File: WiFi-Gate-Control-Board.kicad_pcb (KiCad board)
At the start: 4 copper layers, 139.7 x 158.8 mm, 259 parts, among them J1 USB_B_Micro, J10 Screw_Terminal_01x02, J11 Screw_Terminal_01x04, J12 Screw_Terminal_01x04, J2 Cortex Debug, J3 Motor, J4 Screw_Terminal_01x04, J5 Screw_Terminal_01x04, J6 Screw_Terminal_01x04, J7 Screw_Terminal_01x04, J8 Screw_Terminal_01x04, J9 Screw_Terminal_01x04, Q1 IPD90P03P4L-04, Q2 IFX007T, Q3 IFX007T, SW1 LED Enable, SW2 Open-Close, U1 LMZ21700, U10 TPS3779, U11 TPS3779, U12 TPS3779, U13 TPS3779, U14 TCA6424A, U15 REF3330, U16 TPS3779, U17 TPS3779, U18 TPS3779, U19 TPS3779, U2 DS18B20U, U20 TPS3779, U21 TPS3779, U22 TPS3779, U23 TPS3779, U24 LMZ21700, U25 LP5024, U26 TCA6408A, U27 ITS4075Q, U3 ATWINC1500-MR210UB, U4 SAMD21G18-M, U5 74LVC2G07, U6 74LVC2G06, U7 74LVC2G17, U8 74LVC1G04, U9 REF3325, Y1 32.768kHz

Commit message: Rev 1.0 Release
Added input design and calculations. Added BOM. Added Fuse 3D Model.
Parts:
- removed the J11 at (218.8, 173.2)
- removed the J6 at (106.4, 164.3)
- added J5: Screw_Terminal_01x04, Connector_Phoenix_MSTB:PhoenixContact_MSTBVA_2,5_4-G-5,08_1x04_P5.08mm_Vertical, F.Cu at (106.4, 164.3)
- added J9: Screw_Terminal_01x02, Connector_Phoenix_MSTB:PhoenixContact_MSTBVA_2,5_2-G-5,08_1x02_P5.08mm_Vertical, F.Cu at (194.6, 199.2)
- D28: renamed from D7; footprint Package_TO_SOT_SMD:SOT-23 -> Package_TO_SOT_SMD:SOT-323_SC-70
- J10: value Screw_Terminal_01x02 -> Screw_Terminal_01x04; footprint Connector_Phoenix_MSTB:PhoenixContact_MSTBVA_2,5_2-G-5,08_1x02_P5.08mm_Vertical -> Connector_Phoenix_MSTB:PhoenixContact_MSTBVA_2,5_4-G-5,08_1x04_P5.08mm_Vertical
- Z1: footprint Diode_SMD:D_SOD-523 -> Diode_SMD:D_SOT-23_ANK
- moved J10 35.5 mm to (218.8, 173.2), turned to 270 degrees
- moved Z1 2.43 mm to (175.2, 65.9), turned to 0 degrees
- renumbered C42 to C25, C43 to C26, C44 to C27, C45 to C28, C46 to C29, C47 to C30, C48 to C31, C49 to C32, C50 to C33, C51 to C34, C52 to C35, C53 to C36, C54 to C37, C55 to C38, C56 to C39, C57 to C40, C58 to C41, C59 to C42, C60 to C43, C61 to C44, C62 to C45, C63 to C46, C64 to C47, C65 to C48, C66 to C49, C67 to C50, C68 to C51, C69 to C52, C70 to C53, C71 to C54, C72 to C55, C73 to C56, C74 to C57, C75 to C58, C76 to C59, C77 to C60, C78 to C61, C79 to C62, C80 to C63, C25 to C64, C26 to C65, C27 to C66, C28 to C67, C29 to C68, C30 to C69, C31 to C70, C32 to C71, C33 to C72, C34 to C73, C35 to C74, C36 to C75, C37 to C76, C38 to C77, C39 to C78, C40 to C79, C41 to C80, D11 to D10, D12 to D11, D13 to D12, D14 to D13, D15 to D14, D16 to D15, D17 to D16, D18 to D17, D19 to D18, D20 to D19, D21 to D20, D22 to D21, D23 to D22, D24 to D23, D25 to D24, D26 to D25, D27 to D26, D28 to D27, D8 to D7, D9 to D8, D10 to D9, F2 to F1, F3 to F2, F1 to F3, J12 to J11, J3 to J12, J4 to J3, J5 to J4, J7 to J6, J8 to J7, J9 to J8, R22 to R10, R23 to R11, R24 to R12, R25 to R13, R26 to R14, R27 to R15, R28 to R16, R29 to R17, R30 to R18, R31 to R19, R32 to R20, R33 to R21, R34 to R22, R35 to R23, R36 to R24, R37 to R25, R38 to R26, R39 to R27, R40 to R28, R41 to R29, R42 to R30, R43 to R31, R44 to R32, R45 to R33, R46 to R34, R47 to R35, R48 to R36, R49 to R37, R50 to R38, R51 to R39, R52 to R40, R53 to R41, R54 to R42, R55 to R43, R56 to R44, R57 to R45, R58 to R46, R59 to R47, R60 to R48, R61 to R49, R62 to R50, R63 to R51, R64 to R52, R65 to R53, R66 to R54, R67 to R55, R68 to R56, R69 to R57, R70 to R58, R71 to R59, R72 to R60, R73 to R61, R74 to R62, R75 to R63, R76 to R64, R77 to R65, R78 to R66, R79 to R67, R80 to R68, R81 to R69, R82 to R70, R83 to R71, R84 to R72, R85 to R73, R86 to R74, R10 to R75, R11 to R76, R12 to R77, R13 to R78, R14 to R79, R15 to R80, R16 to R81, R17 to R82, R18 to R83, R19 to R84, R20 to R85, R21 to R86, U13 to U10, U14 to U11, U15 to U12, U16 to U13, U17 to U14, U18 to U15, U19 to U16, U20 to U17, U21 to U18, U22 to U19, U23 to U20, U24 to U21, U25 to U22, U26 to U23, U27 to U24, U7 to U25, U8 to U26, U9 to U27, U10 to U7, U11 to U8, U12 to U9
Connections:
- J10 pad 1: GND -> /Outputs and LEDs/VSW3
- J10 pad 2: /Outputs and LEDs/VSW2 -> GND
- RL1 pad 3: Net-(J11-Pad3) (its old number) -> Net-(J10-Pad3)
- RL1 pad 4: Net-(J11-Pad4) (its old number) -> Net-(J10-Pad4)
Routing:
- net Net-(J11-Pad4) (its old number): track 13.3 -> 0.00 mm
- net Net-(J11-Pad3) (its old number): track 13.3 -> 0.00 mm
- net Net-(J10-Pad4): track 0.00 -> 13.3 mm
- net Net-(J10-Pad3): track 0.00 -> 13.3 mm
- net Net-(D28-Pad1): track 19.8 -> 22.4 mm
- net Net-(Q1-Pad1): track 4.79 -> 6.76 mm
- net GND: track 245.0 -> 246.8 mm, vias 171 -> 252
- net +3.3V: track 135.7 -> 136.3 mm
- net /Inputs/IN11: track 15.8 -> 16.3 mm
- net /Motor Driver/M1B: vias 55 -> 47
- net /Motor Driver/M1A: vias 54 -> 46
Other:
- board text removed: "Radio"

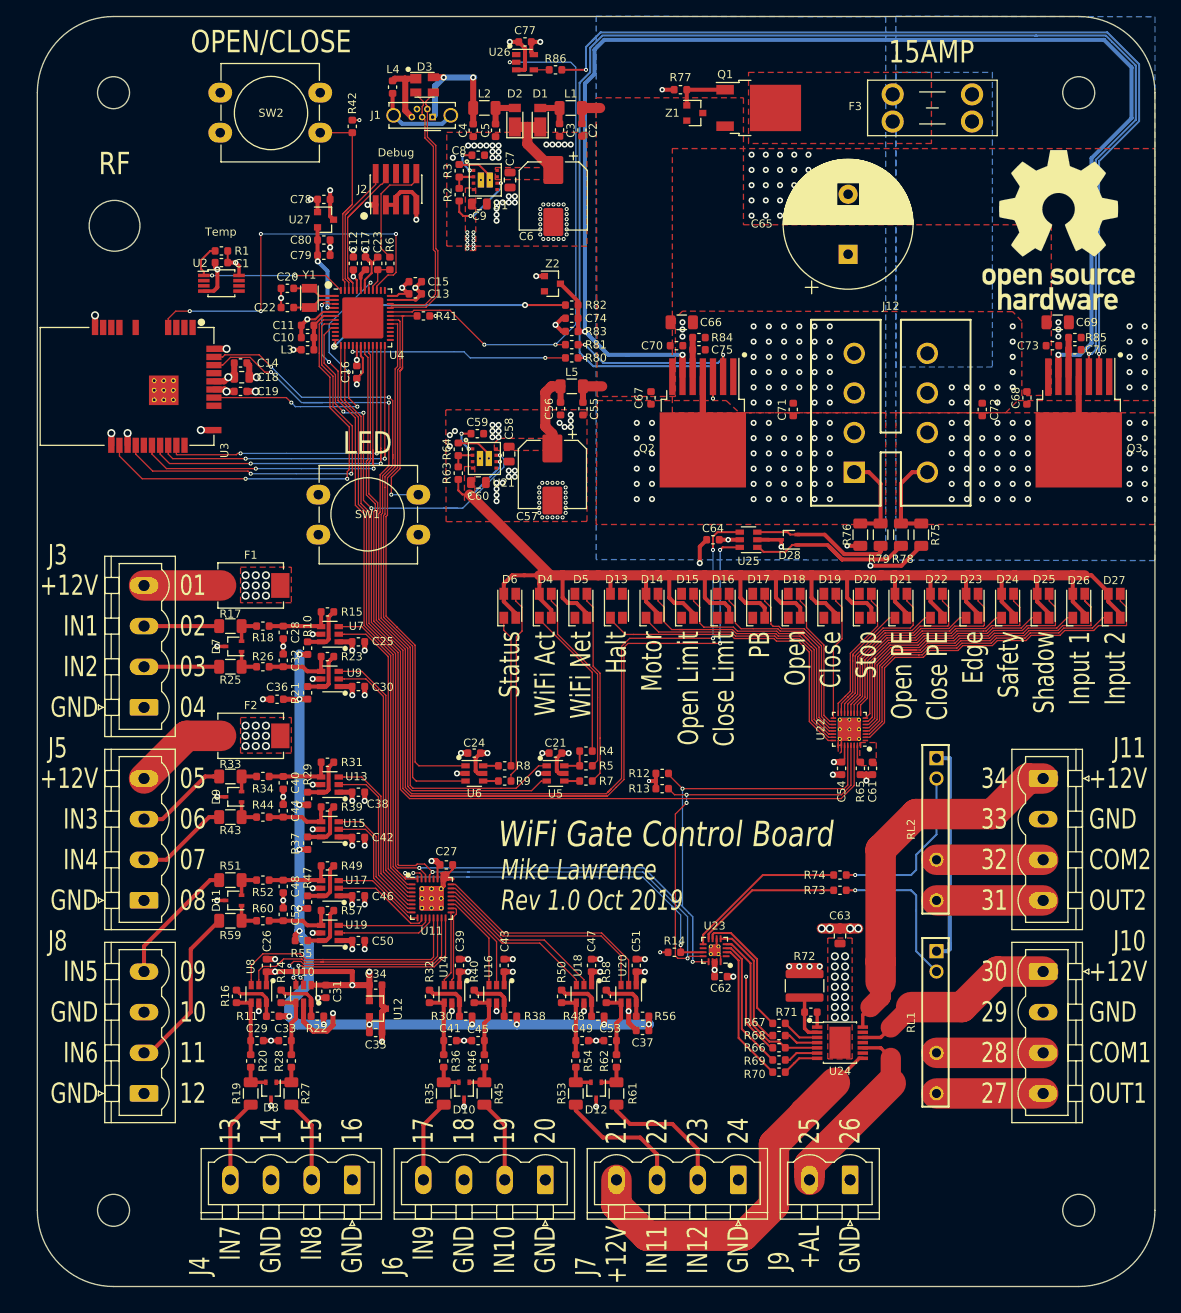
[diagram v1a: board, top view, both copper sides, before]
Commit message: PCB to Rev 1.1
Fixed missing Reference Designators on top Silkscreen.
Reset input on TCA6424A and TCA6408A now connected to 3.3V.
Added series Schottky Diode to LED power supply input.
Replaced 1000uF main power capacitor with two 470uF capacitors.
Replaced DS18B20 temperature sensor with TMP100 temperature sensor.
Increased LED currents to 25mA
Removed U26 inverter and connected U3 IN pin directly to processor. Now able to measure unloaded offset current.
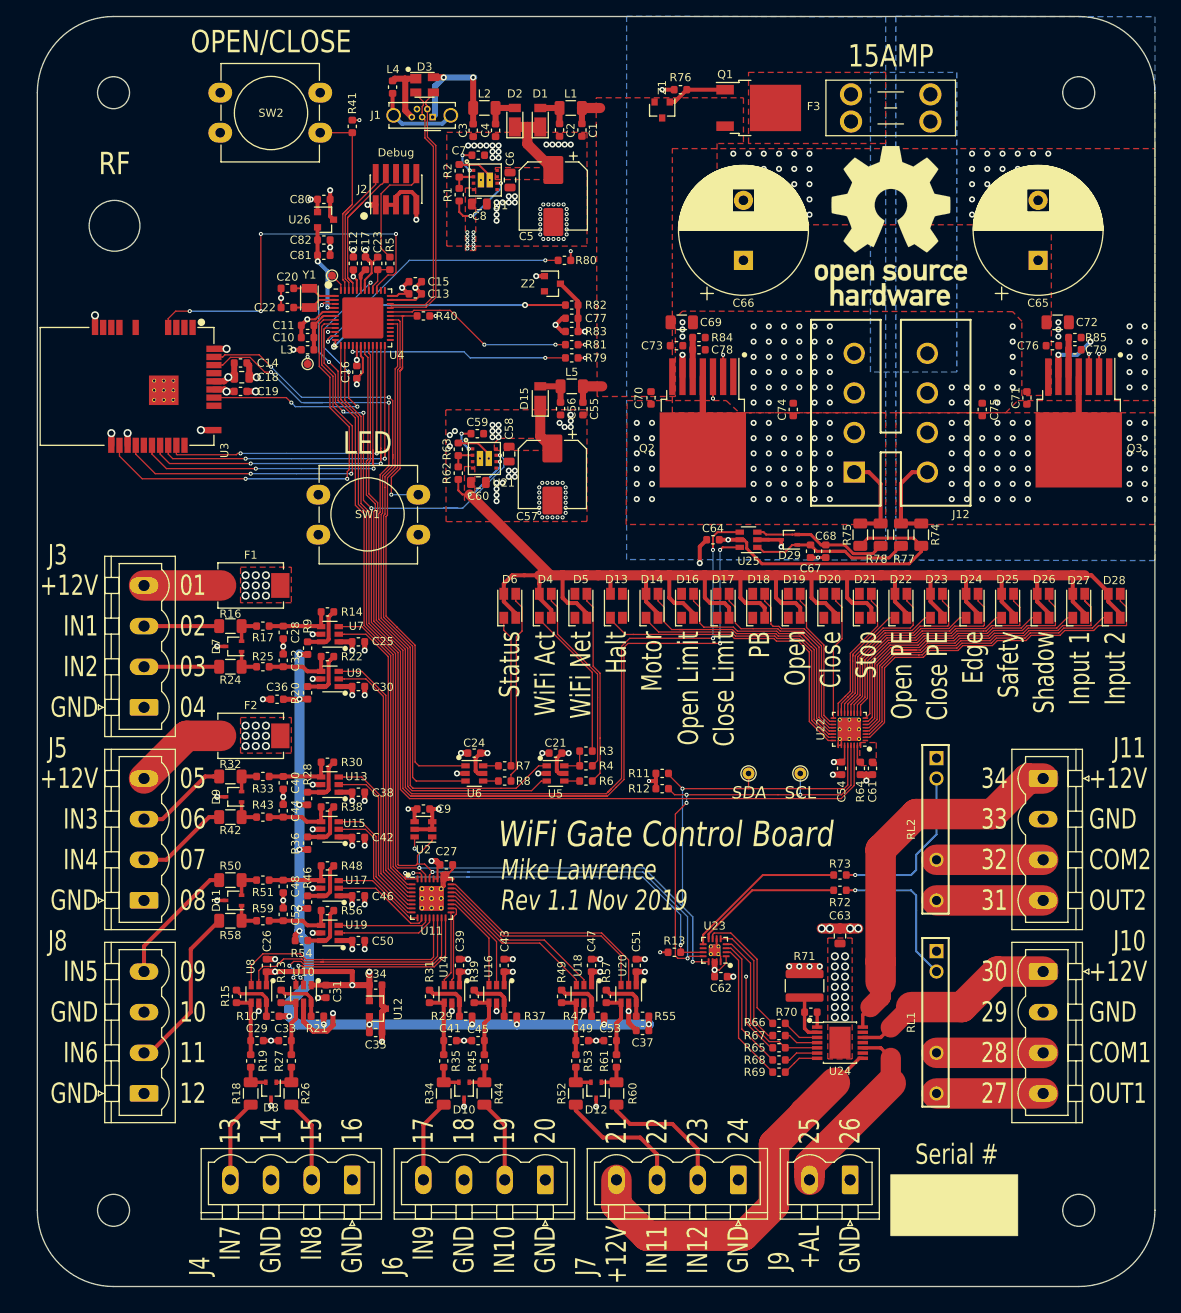
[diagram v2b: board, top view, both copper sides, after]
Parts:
- removed the C1 at (116.0, 84.6)
- removed the C77 at (154.0, 57.0)
- removed the D18 at (187.6, 127.5)
- removed the D27 at (227.6, 127.5)
- removed the R1 at (116.0, 83.1)
- removed the R12 at (171.1, 148.4)
- removed the R28 at (124.8, 184.4)
- removed the R69 at (185.7, 184.3)
- removed the R73 at (193.4, 163.0)
- removed the R76 at (195.9, 118.6)
- removed the R8 at (151.4, 147.5)
- removed R86: 10k, Resistor_SMD:R_0603_1608Metric
- removed the U26 at (154.0, 59.5)
- added C66: 470uF, Capacitor_THT:CP_Radial_D16.0mm_P7.50mm, F.Cu at (181.3, 84.3)
- added C67: DNI, Capacitor_SMD:C_0603_1608Metric, F.Cu at (189.7, 120.7)
- added C68: DNI, Capacitor_SMD:C_0603_1608Metric, F.Cu at (191.6, 120.7)
- added C9: 0.1uF, Capacitor_SMD:C_0603_1608Metric, F.Cu at (141.3, 152.9)
- added D15: DFLS130, Diode_SMD:D_PowerDI-123, F.Cu at (155.9, 101.6)
- added D19: Red/Green, LED_SMD:LED_Avago_PLCC4_3.2x2.8mm_CW, F.Cu at (187.6, 127.5)
- added D28: Red/Green, LED_SMD:LED_Avago_PLCC4_3.2x2.8mm_CW, F.Cu at (227.6, 127.5)
- added R10: 33.2k, Resistor_SMD:R_0603_1608Metric, F.Cu at (122.4, 178.8)
- added R27: 10k, Resistor_SMD:R_0603_1608Metric, F.Cu at (124.8, 184.4)
- added R68: 10k, Resistor_SMD:R_0603_1608Metric, F.Cu at (185.7, 184.3)
- added R7: 44.2R, Resistor_SMD:R_0603_1608Metric, F.Cu at (151.4, 147.5)
- added R72: 422R, Resistor_SMD:R_0603_1608Metric, F.Cu at (193.4, 163.0)
- added R75: 330k, Resistor_SMD:R_1206_3216Metric, F.Cu at (195.9, 118.6)
- added R80: 10k, Resistor_SMD:R_0603_1608Metric, F.Cu at (158.9, 84.3)
- added TP1: TestPoint_Probe, TestPoint:TestPoint_Pad_D1.0mm, F.Cu at (129.9, 86.2)
- added TP2: TestPoint_Probe, TestPoint:TestPoint_Pad_D1.0mm, F.Cu at (126.8, 97.3)
- added TP3: SDA, TestPoint:TestPoint_THTPad_D1.5mm_Drill0.7mm, F.Cu at (181.9, 148.4)
- added TP4: SCL, TestPoint:TestPoint_THTPad_D1.5mm_Drill0.7mm, F.Cu at (188.4, 148.4)
- C65: value 1000uF -> 470uF
- J10, J11, J3, J4, J5, J6, J7, J8: value Screw_Terminal_01x04 -> Screw Header 4 Pos
- J9: value Screw_Terminal_01x02 -> Screw Header 2 Pos
- R11: value 33.2k -> 4.7k
- R3: renamed from R4; value 143R -> 44.2R
- R4: renamed from R5; value 143R -> 44.2R
- R6: renamed from R7; value 73.2R -> 44.2R
- R64: renamed from R65; value 3.74k -> 2.94k
- R8: renamed from R9; value 73.2R -> 44.2R
- U2: value DS18B20U -> TMP100; footprint Package_SO:MSOP-8_3x3mm_P0.65mm -> Package_TO_SOT_SMD:SOT-23-6
- moved U2 72.8 mm to (141.3, 155.4), turned to 180 degrees
- moved R11 57.4 mm to (171.1, 148.4), turned to 0 degrees
- moved C65 23.8 mm to (218.1, 84.3)
- moved REF** 21.0 mm to (199.7, 80.0)
- moved F3 5.21 mm to (204.7, 67.0)
- moved Z1 4.09 mm to (171.1, 65.5), turned to 270 degrees
- renumbered C2 to C1, C3 to C2, C4 to C3, C5 to C4, C6 to C5, C7 to C6, C66 to C69, C8 to C7, C67 to C70, C68 to C71, C69 to C72, C70 to C73, C71 to C74, C72 to C75, C73 to C76, C74 to C77, C75 to C78, C76 to C79, C9 to C8, C78 to C80, C79 to C81, C80 to C82, D15 to D16, D16 to D17, D17 to D18, D19 to D20, D20 to D21, D21 to D22, D22 to D23, D23 to D24, D24 to D25, D25 to D26, D26 to D27, D28 to D29, R2 to R1, R13 to R12, R14 to R13, R15 to R14, R16 to R15, R17 to R16, R18 to R17, R19 to R18, R20 to R19, R3 to R2, R21 to R20, R22 to R21, R23 to R22, R24 to R23, R25 to R24, R26 to R25, R27 to R26, R29 to R28, R30 to R29, R31 to R30, R32 to R31, R33 to R32, R34 to R33, R35 to R34, R36 to R35, R37 to R36, R38 to R37, R39 to R38, R40 to R39, R41 to R40, R42 to R41, R43 to R42, R44 to R43, R45 to R44, R46 to R45, R47 to R46, R48 to R47, R49 to R48, R50 to R49, R6 to R5, R51 to R50, R52 to R51, R53 to R52, R54 to R53, R55 to R54, R56 to R55, R57 to R56, R58 to R57, R59 to R58, R60 to R59, R61 to R60, R62 to R61, R63 to R62, R64 to R63, R66 to R65, R67 to R66, R68 to R67, R70 to R69, R71 to R70, R72 to R71, R74 to R73, R75 to R74, R77 to R76, R78 to R77, R79 to R78, R80 to R79, R10 to R9, Ref** to RF, U27 to U26
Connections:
- C57 pad 1: Net-(C56-Pad2) -> Net-(C57-Pad1)
- C58 pad 1: Net-(C56-Pad2) -> Net-(C57-Pad1)
- R11 pad 1: +3.0V -> +3.3V
- R11 pad 2: Net-(R11-Pad2) -> SDA
- R15 pad 2: Net-(R11-Pad2) -> Net-(R10-Pad2)
- U11 pad 28: (no net) -> +3.3V
- U2 pad 1: A2 -> SCL
- U2 pad 2: (no net) -> GND
- U2 pad 3: (no net) -> GND
- U2 pad 4: GND -> +3.3V
- U2 pad 5: (no net) -> GND
- U2 pad 6: (no net) -> SDA
- U21 pad 8: Net-(C56-Pad2) -> Net-(C57-Pad1)
- U23 pad 1: (no net) -> +3.3V
- U4 pad 10: (no net) -> A4
- U4 pad 11: (no net) -> A5
- U8 pad 6: Net-(R11-Pad2) -> Net-(R10-Pad2)
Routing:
- net D1: track 68.8 -> 23.8 mm, vias 3 -> 2
- net A5: track 0.00 -> 34.4 mm, vias 0 -> 2
- net GND: track 246.8 -> 214.0 mm, vias 252 -> 281
- net +3.3V: track 136.3 -> 160.3 mm, vias 50 -> 47
- net Net-(Q3-Pad2): track 119.3 -> 140.9 mm
- net A2: track 22.2 -> 2.31 mm, vias 2 -> 0
- net Net-(C56-Pad2): track 11.6 -> 4.54 mm
- net SCL: track 166.3 -> 173.1 mm, vias 4 -> 5
- net Net-(R11-Pad2): track 6.42 -> 0.00 mm
- net Net-(R10-Pad2): track 0.00 -> 6.42 mm
- net SDA: track 165.7 -> 171.8 mm, vias 3 -> 4
- net Net-(C57-Pad1): track 0.00 -> 6.02 mm
- net A4: track 0.00 -> 5.98 mm, vias 0 -> 2
- net Net-(C77-Pad1): track 172.7 -> 174.9 mm, vias 3 -> 4
- net Net-(R86-Pad2): track 1.92 -> 0.00 mm
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- added copper zone on F.Cu, net Net-(C57-Pad1)
- removed copper zone on F.Cu, net Net-(C56-Pad2)
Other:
- board text added: "Rev 1.1 Nov 2019"
- board text added: "Serial #"
- board text removed: "Rev 1.0 Oct 2019"
- board text removed: "Temp"

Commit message: Changed Cortex Debug connector. Added fabrication pdf.
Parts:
- SW1: value LED Enable -> ~
- SW2: value Open-Close -> ~
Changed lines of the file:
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@@
     (nets 201)
   )
-  (page A3)
+  (page A3 portrait)
   (layers
     (0 F.Cu signal)
@@
     (visible_elements 7FFDFF7F)
     (pcbplotparams
-      (layerselection 0x010fc_ffffffff)
+      (layerselection 0x20000_7ffffff8)
       (usegerberextensions true)
       (usegerberattributes false)
@@
       (plotvalue false)
       (plotinvisibletext false)
-      (padsonsilk false)
+      (padsonsilk true)
       (subtractmaskfromsilk false)
-      (outputformat 1)
+      (outputformat 5)
       (mirror false)
       (drillshape 0)
@@
     (add_net /Inputs/IN9SEN0)
     (add_net /Inputs/IN9SEN1)
+    (add_net /MISO)
+    (add_net /MOSI)
     (add_net "/Motor Driver/M1A")
     (add_net "/Motor Driver/M1B")
@@
     (add_net "/Outputs and LEDs/VSW4EN")
     (add_net "/Outputs and LEDs/~VSWERR")
+    (add_net /RX)
+    (add_net /SCK)
     (add_net /SWCLK)
     (add_net /SWDIO)
+    (add_net /TX)
+    (add_net /USB_ID)
     (add_net /USB_N)
     (add_net /USB_P)
@@
     (add_net D0)
     (add_net D1)
+    (add_net D2)
     (add_net D3)
     (add_net D4)
@@
     (add_net "Net-(D12-Pad2)")
     (add_net "Net-(D13-Pad1)")
+    (add_net "Net-(D13-Pad3)")
+    (add_net "Net-(D13-Pad4)")
     (add_net "Net-(D14-Pad1)")
     (add_net "Net-(D14-Pad3)")
+    (add_net "Net-(D16-Pad1)")
+    (add_net "Net-(D16-Pad2)")
     (add_net "Net-(D16-Pad3)")
+    (add_net "Net-(D17-Pad1)")
+    (add_net "Net-(D17-Pad2)")
     (add_net "Net-(D17-Pad3)")
+    (add_net "Net-(D18-Pad1)")
+    (add_net "Net-(D18-Pad2)")
     (add_net "Net-(D18-Pad3)")
+    (add_net "Net-(D19-Pad1)")
+    (add_net "Net-(D19-Pad2)")
     (add_net "Net-(D19-Pad3)")
+    (add_net "Net-(D20-Pad1)")
+    (add_net "Net-(D20-Pad2)")
     (add_net "Net-(D20-Pad3)")
+    (add_net "Net-(D21-Pad1)")
+    (add_net "Net-(D21-Pad2)")
     (add_net "Net-(D21-Pad3)")
     (add_net "Net-(D22-Pad1)")
@@
     (add_net "Net-(D4-Pad1)")
     (add_net "Net-(D4-Pad3)")
+    (add_net "Net-(D5-Pad1)")
+    (add_net "Net-(D5-Pad2)")
     (add_net "Net-(D5-Pad3)")
     (add_net "Net-(D6-Pad1)")
@@
     (add_net "Net-(F2-Pad2)")
     (add_net "Net-(F3-Pad2)")
+    (add_net "Net-(J1-Pad4)")
     (add_net "Net-(J1-Pad6)")
     (add_net "Net-(J10-Pad3)")
@@
     (add_net "Net-(J12-Pad1)")
     (add_net "Net-(J12-Pad2)")
+    (add_net "Net-(J12-Pad6)")
     (add_net "Net-(J2-Pad10)")
+    (add_net "Net-(J2-Pad6)")
+    (add_net "Net-(J2-Pad7)")
+    (add_net "Net-(J2-Pad8)")
     (add_net "Net-(Q1-Pad1)")
     (add_net "Net-(Q2-Pad2)")
@@
     (add_net "Net-(R73-Pad2)")
     (add_net "Net-(R8-Pad2)")
+    (add_net "Net-(U1-Pad3)")
+    (add_net "Net-(U21-Pad3)")
+    (add_net "Net-(U22-Pad1)")
+    (add_net "Net-(U23-Pad10)")
+    (add_net "Net-(U3-Pad1)")
+    (add_net "Net-(U3-Pad14)")
+    (add_net "Net-(U3-Pad19)")
+    (add_net "Net-(U3-Pad2)")
+    (add_net "Net-(U3-Pad21)")
+    (add_net "Net-(U3-Pad25)")
     (add_net "Net-(U3-Pad26)")
     (add_net "Net-(U3-Pad27)")
+    (add_net "Net-(U3-Pad3)")
     (add_net SCL)
     (add_net SDA)
@@
       (effects (font (size 1 1) (thickness 0.15)))
     )
-    (fp_text value DNI (at 0 1.43 90) (layer F.Fab)
+    (fp_text value DNI (at 0 1.43 90) (layer F.Fab) hide
       (effects (font (size 1 1) (thickness 0.15)))
     )
@@
       (effects (font (size 1 1) (thickness 0.15)))
     )
-    (fp_text value DNI (at 0 1.43 90) (layer F.Fab)
+    (fp_text value DNI (at 0 1.43 90) (layer F.Fab) hide
       (effects (font (size 1 1) (thickness 0.15)))
     )
@@
       (effects (font (size 1 1) (thickness 0.15)))
     )
-    (fp_text value TestPoint_Probe (at 0 1.55) (layer F.Fab)
+    (fp_text value TestPoint_Probe (at 0 1.55) (layer F.Fab) hide
       (effects (font (size 1 1) (thickness 0.15)))
     )
@@
       (effects (font (size 1 1) (thickness 0.15)))
     )
-    (fp_text value TestPoint_Probe (at 0 1.55) (layer F.Fab)
+    (fp_text value TestPoint_Probe (at 0 1.55) (layer F.Fab) hide
       (effects (font (size 1 1) (thickness 0.15)))
     )
@@
       (effects (font (size 1.016 1.016) (thickness 0.1524)))
     )
-    (fp_text value TMP100 (at 0 2.9) (layer F.Fab)
+    (fp_text value TMP100 (at 0 2.9) (layer F.Fab) hide
       (effects (font (size 1 1) (thickness 0.15)))
     )
@@
       (effects (font (size 1 1) (thickness 0.15)))
     )
-    (fp_text value 470uF (at 3.75 9.25 90) (layer F.Fab)
+    (fp_text value 470uF (at 3.75 9.25 90) (layer F.Fab) hide
       (effects (font (size 1 1) (thickness 0.15)))
     )
@@
       (effects (font (size 1.016 1.016) (thickness 0.1524)))
     )
-    (fp_text value Open-Close (at 6.35 9.93) (layer F.Fab) hide
+    (fp_text value ~ (at 6.35 9.93) (layer F.Fab) hide
       (effects (font (size 1 1) (thickness 0.15)))
     )
@@
       (effects (font (size 1.016 1.016) (thickness 0.1524)))
     )
-    (fp_text value "LED Enable" (at 6.35 9.93) (layer F.Fab) hide
+    (fp_text value ~ (at 6.35 9.93) (layer F.Fab) hide
       (effects (font (size 1 1) (thickness 0.15)))
     )
@@
       (rotate (xyz 0 0 0))
     )
+    (model ${KIPRJMOD}/packages3d/FTSH-105-01-L-DV-K.stp
+      (offset (xyz 0 0 0.4318))
+      (scale (xyz 1 1 1))
+      (rotate (xyz -90 0 90))
+    )
   )
